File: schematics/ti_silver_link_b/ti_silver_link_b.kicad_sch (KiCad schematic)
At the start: 42 parts, among them P1 Conn_1x5, U1 24LC64, U2 TPS71533__SC70, U3 TUSB3410, U4 IMH8A, Y1 12MHz

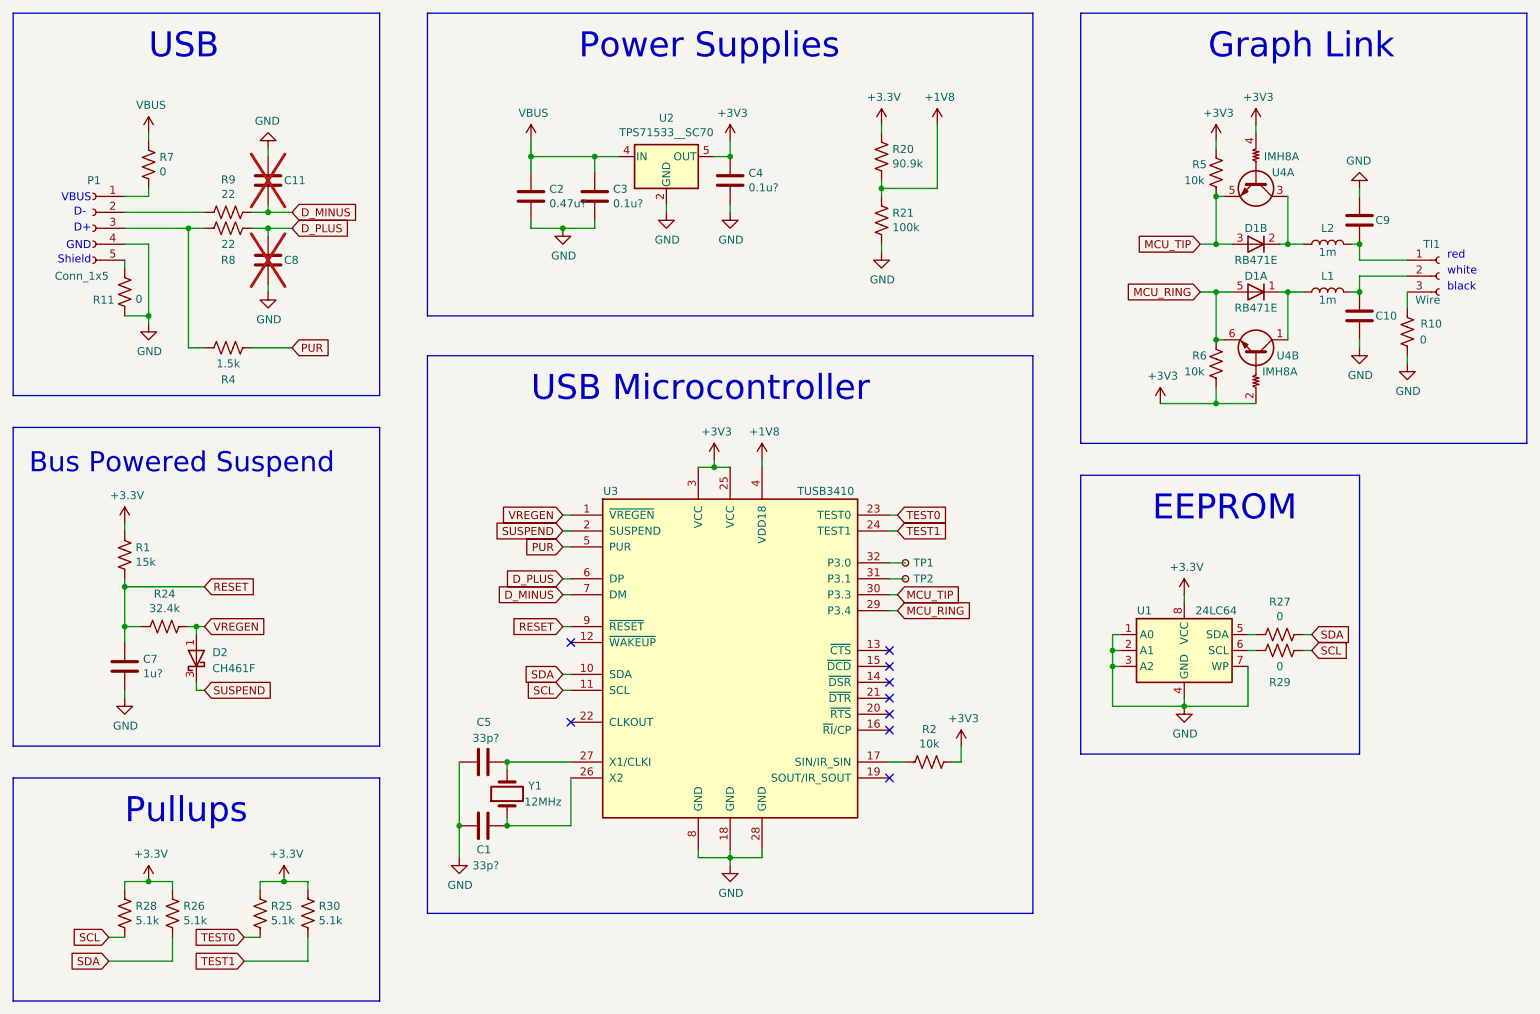
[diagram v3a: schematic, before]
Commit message: Convert all +3.3V nest to +3V3 in TI Silver Link "B" schematic
Addresses issue #3
USB Silver Link "B" schematic had a mix of +3.3V and +3V3 nets.
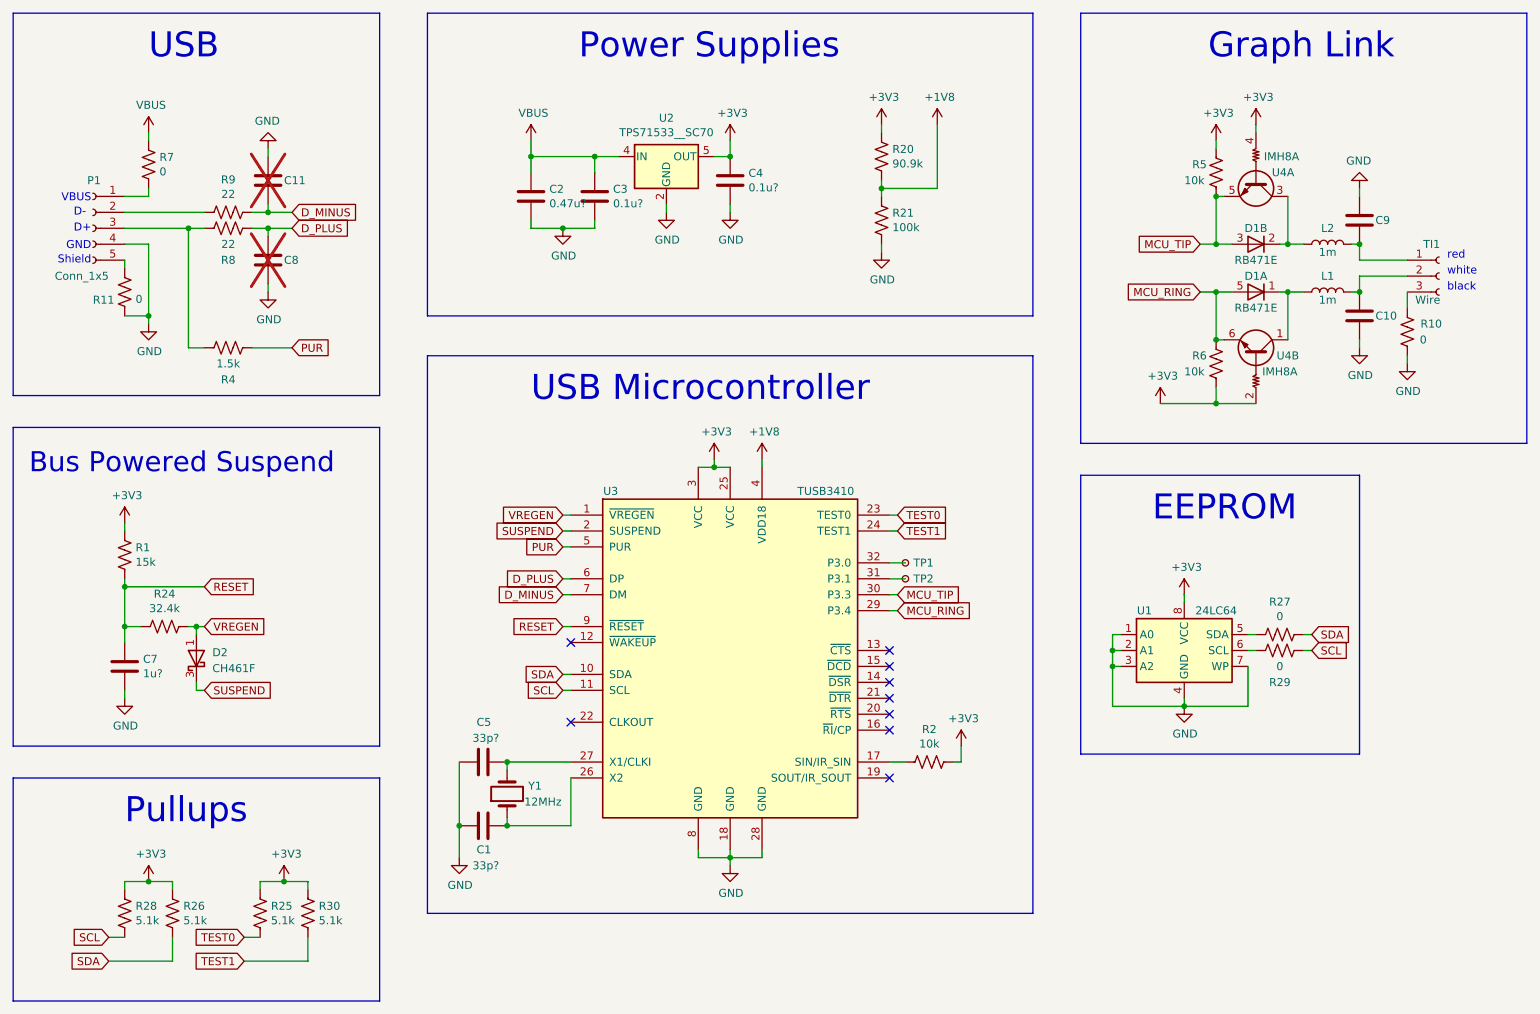
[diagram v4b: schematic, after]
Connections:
- net +3.3V is gone; now on net +3V3: R1.1, R20.1, R25.1, R26.1, R28.1, R30.1, U1.8 (VCC)

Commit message: Move I2C and TEST pullups near their respective devices
 - Move I2C pullups near EEPROM
 - Move TEST pullups near TUSB3410
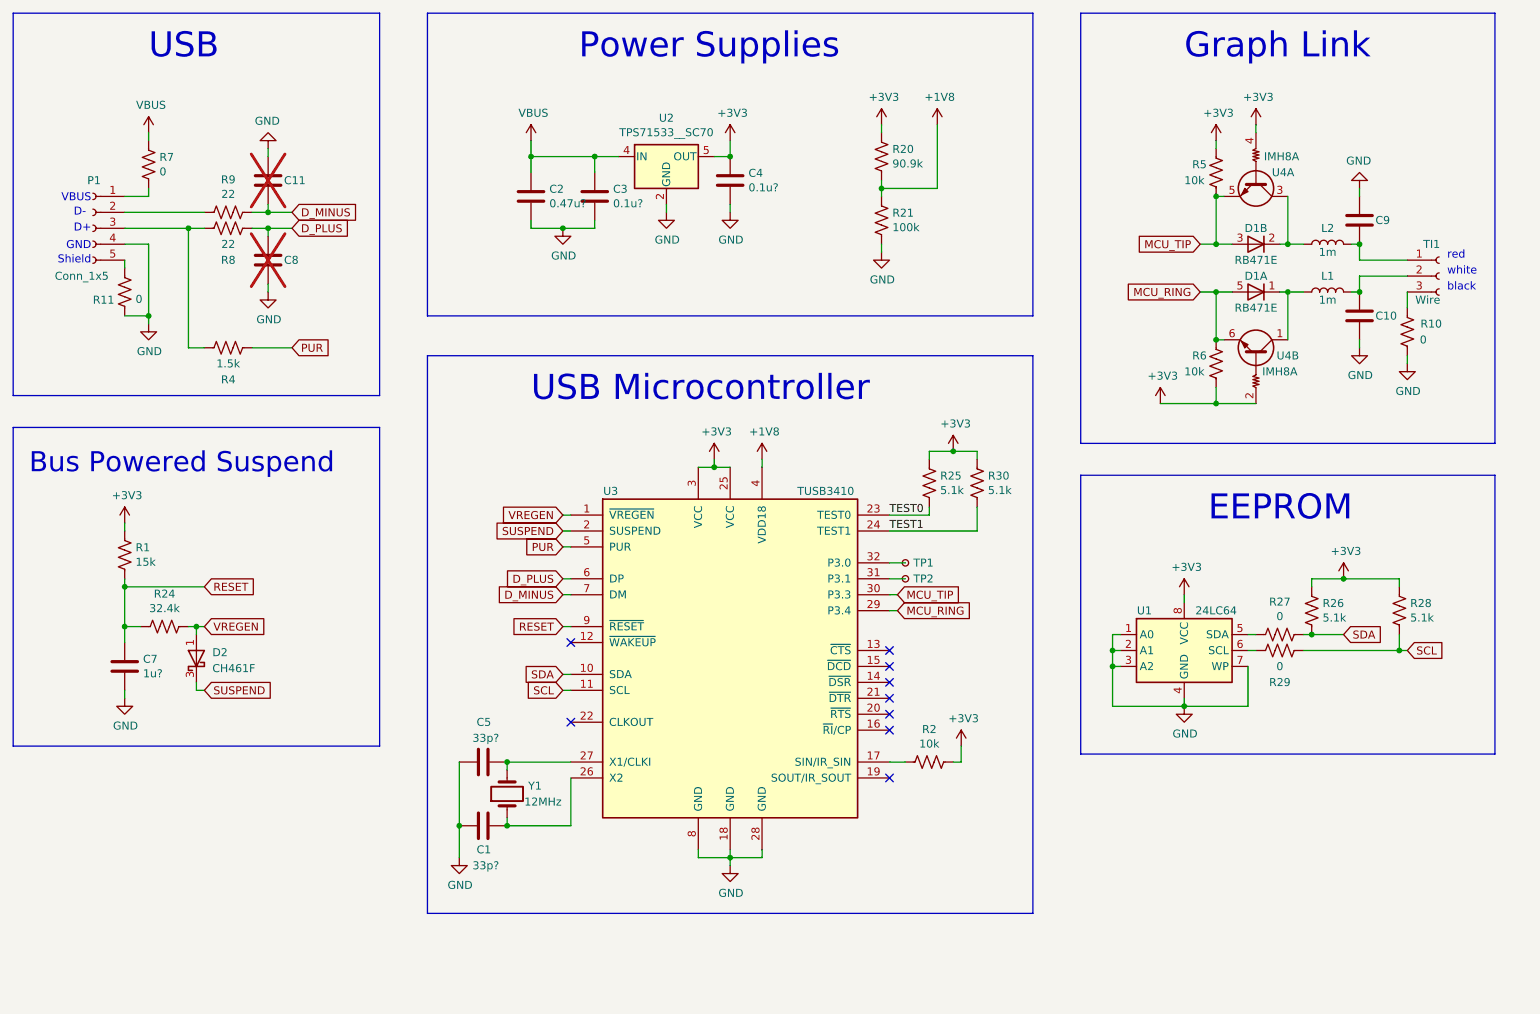
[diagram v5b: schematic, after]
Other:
- note removed: "Pullups"
- moved on the sheet: R25, R26, R28, R30
